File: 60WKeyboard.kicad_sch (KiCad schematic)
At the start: 62 parts, among them IC2 USBLC6-2SC6, J1 USB4215-03-A_REVA, J2 Conn_02x01_MountingPin, J3 Conn_01x04_Socket, U1 PES12-42S-N0024, U3 nRF52840, Y1 ABM11W-32.0000MHZ-7-D1X-T3, Y2 ECS-.327-7-12-TR

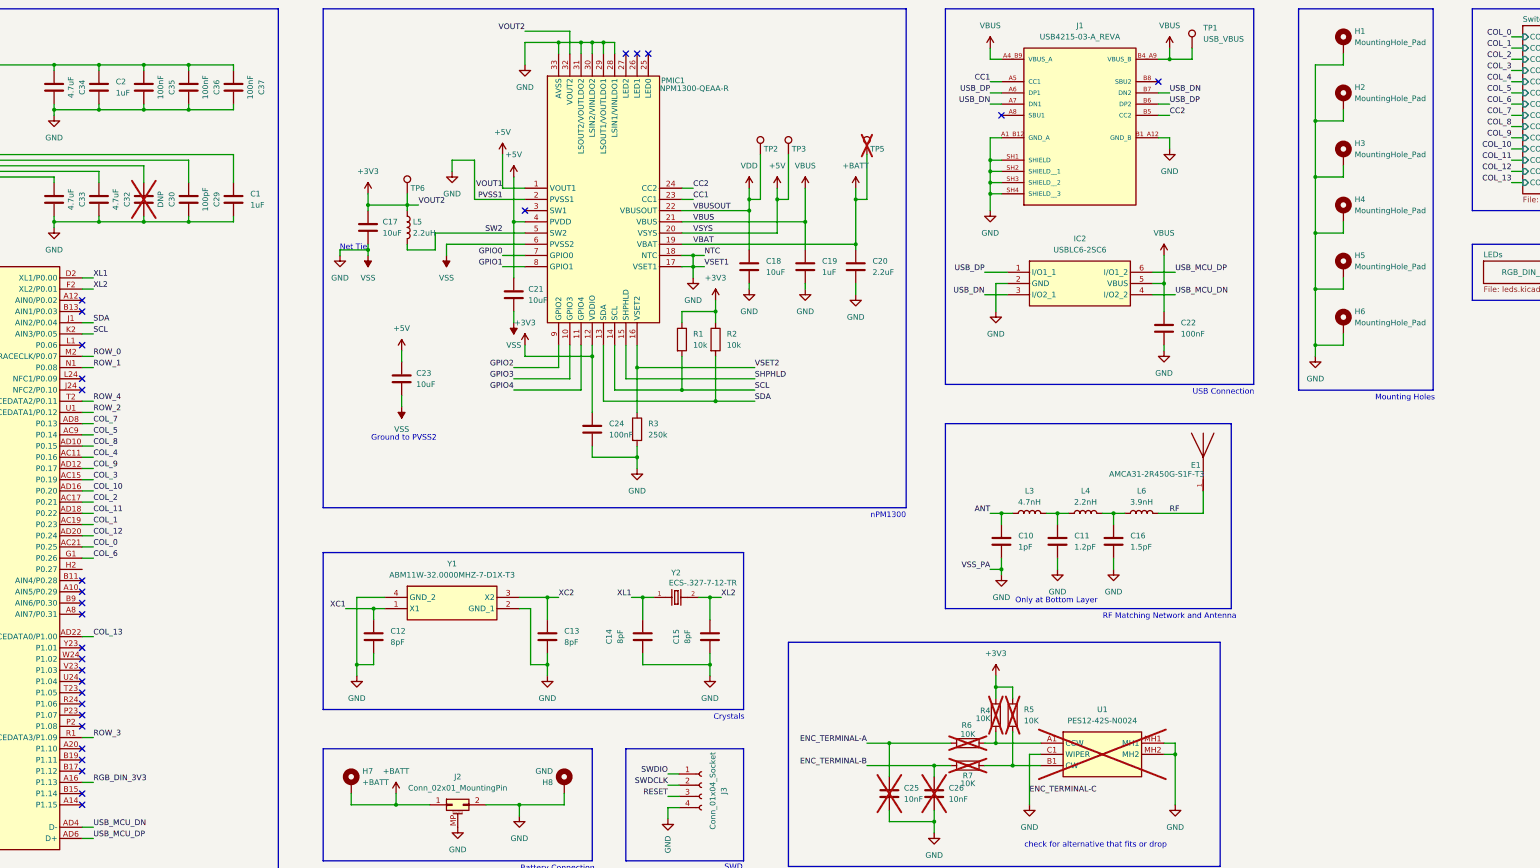
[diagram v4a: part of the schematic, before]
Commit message: Add RGB power control circuit and update PCB
Introduced a new RGB power control circuit using a DMG2301L MOSFET and 10k resistor, connected to the /RGB_POWER net. Updated test point references, modified net assignments, and adjusted routing and vias in the PCB layout. Added and removed backup files and updated production files to reflect the latest design changes.
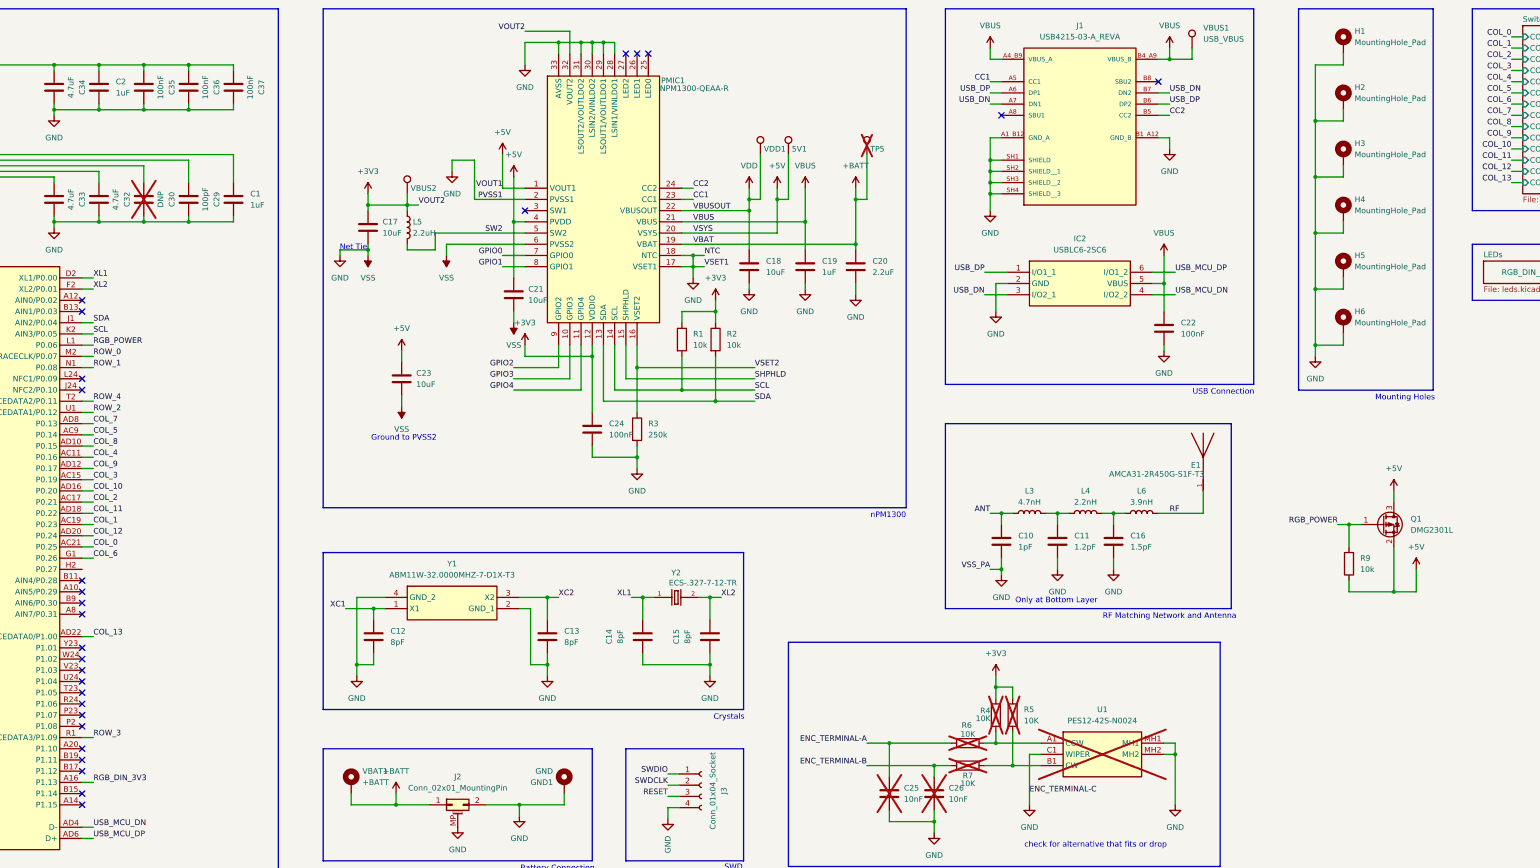
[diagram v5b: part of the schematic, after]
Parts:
- added Q1: DMG2301L, Package_TO_SOT_SMD:SOT-23, symbol Transistor_FET:DMG2301L
- added R9: 10k, Resistor_SMD:R_0402_1005Metric, symbol Device:R
- renumbered TP3 to 5V1, H8 to GND1, H7 to VBAT1, TP1 to VBUS1, TP6 to VBUS2, TP2 to VDD1
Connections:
- net +5V: now also Q1.2 (S), Q1.3 (D), R9.1
- net RGB_POWER: now reaches U3.L1 (P0.06)
- net RGB_POWER: now also Q1.1 (G), R9.2
- no-connect marks 32 -> 31

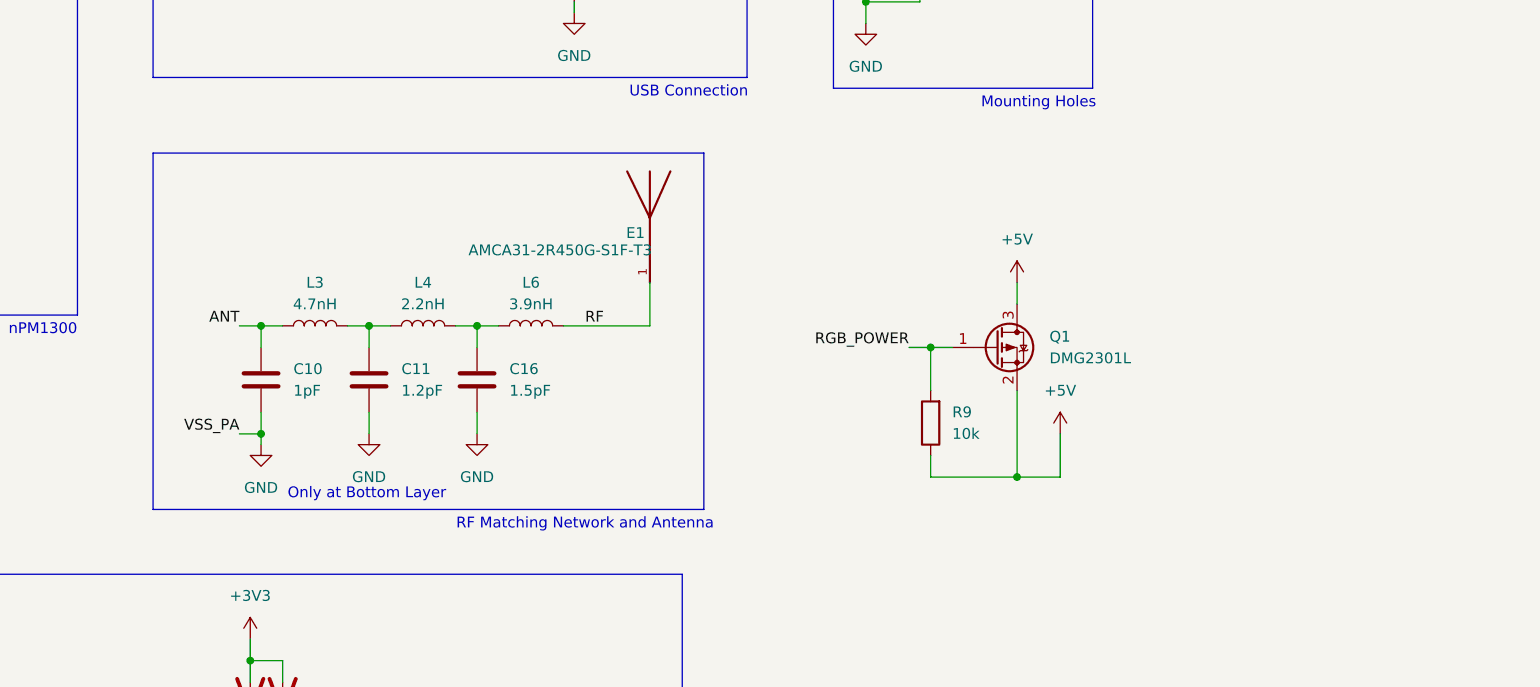
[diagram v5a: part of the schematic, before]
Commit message: Replace RF footprint and add U.FL connector
Replaced the AMCA31-2R450G-S1F-T3 RF footprint with a CONMHF1-SMD-T U.FL connector at the RF output. Updated the S57 keyswitch footprint position. Also updated backup files and production outputs to reflect these changes.
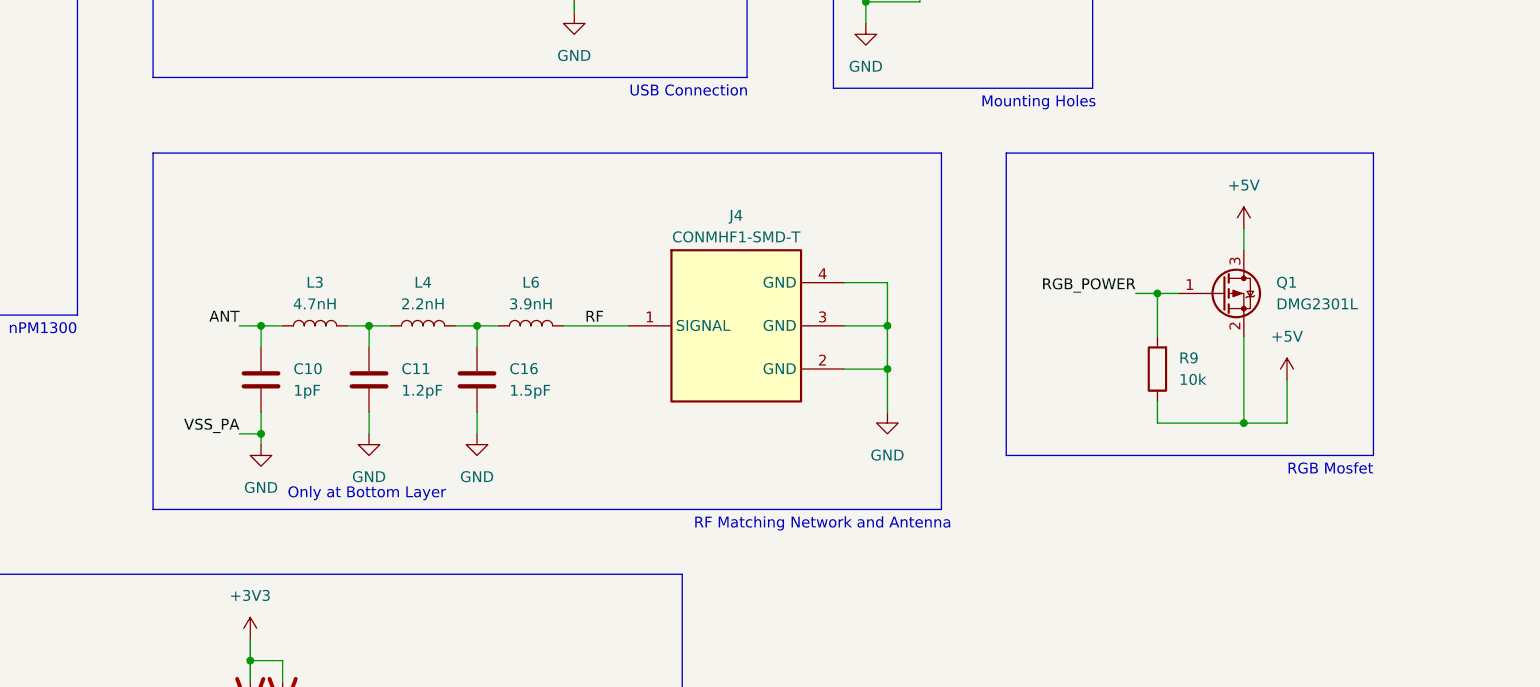
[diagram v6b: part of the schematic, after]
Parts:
- removed E1: AMCA31-2R450G-S1F-T3, SamacSys_Parts:XDCR_AMCA31-2R450G-S1F-T3, symbol AMCA31-2R450G-S1F-T3:AMCA31-2R450G-S1F-T3
- added J4: CONMHF1-SMD-T, CONMHF1SMDT, symbol SamacSys_Parts:CONMHF1-SMD-T
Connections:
- net GND: now also J4.2 (GND), J4.3 (GND), J4.4 (GND)
- net RF: now also J4.1 (SIGNAL)
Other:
- note added: "RGB Mosfet"
- moved on the sheet: Q1, R9

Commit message: Update KiCad project files and backup
Removed autosave and lock files, updated project and schematic files, and renamed backup ZIP. Changed footprint property for connector in schematic and adjusted selection filter for footprints in project settings.
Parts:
- J4: footprint CONMHF1SMDT -> SamacSys_Parts:CONMHF1SMDT
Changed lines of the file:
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@@
 			)
 		)
-		(property "Footprint" "CONMHF1SMDT"
+		(property "Footprint" "SamacSys_Parts:CONMHF1SMDT"
 			(at 434.34 300.66 0)
 			(effects

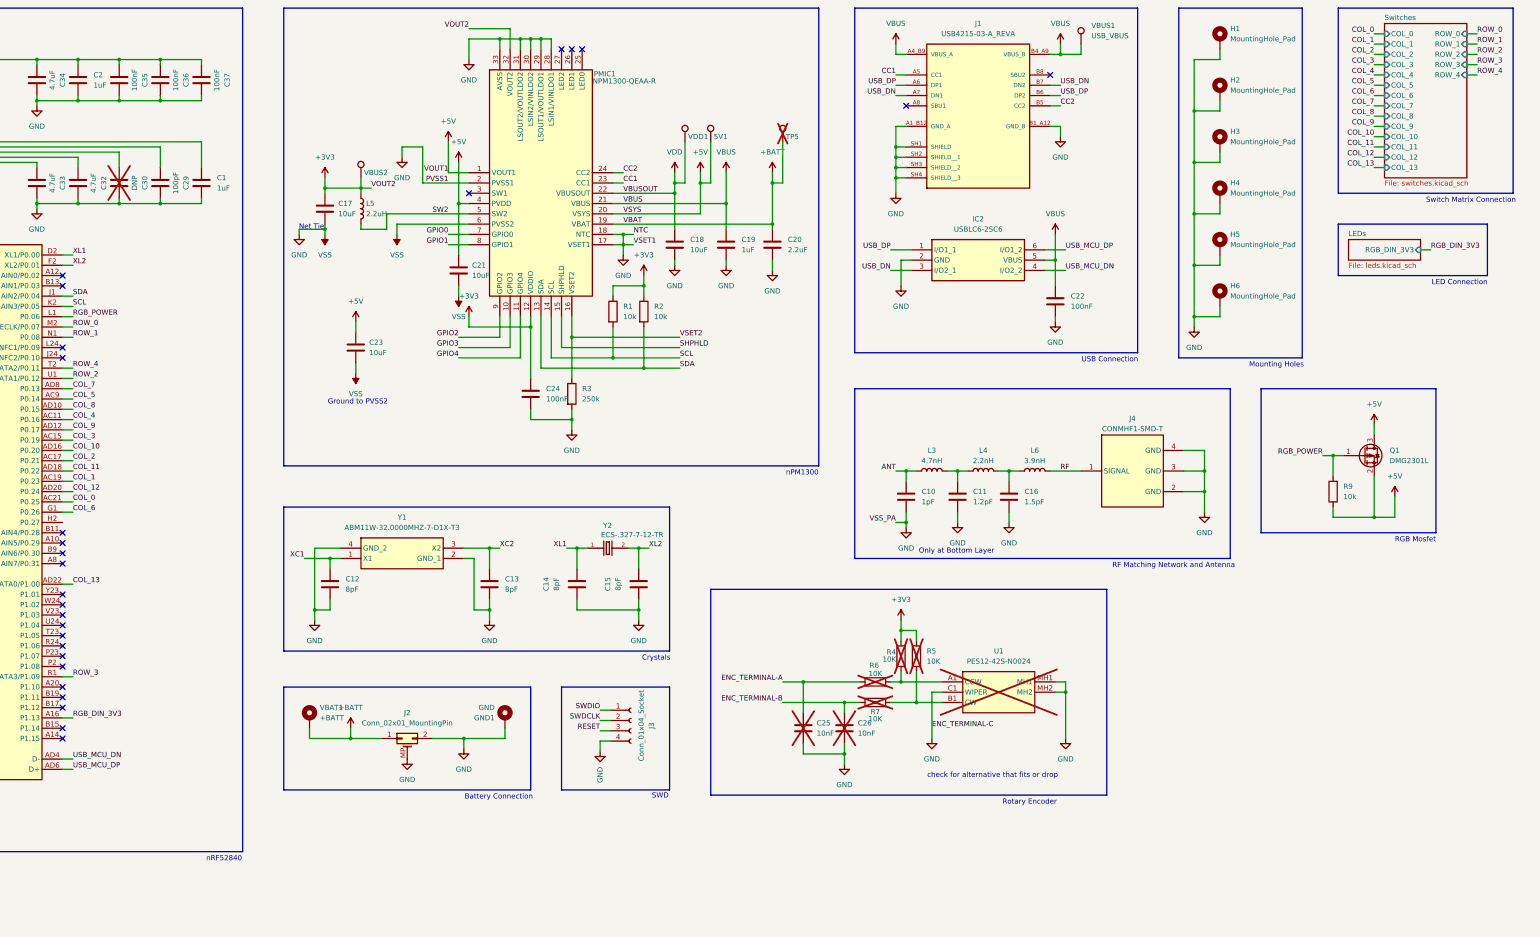
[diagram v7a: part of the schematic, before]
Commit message: v0.4-routing done
need to work on routing and fix it up but preliminary routing done
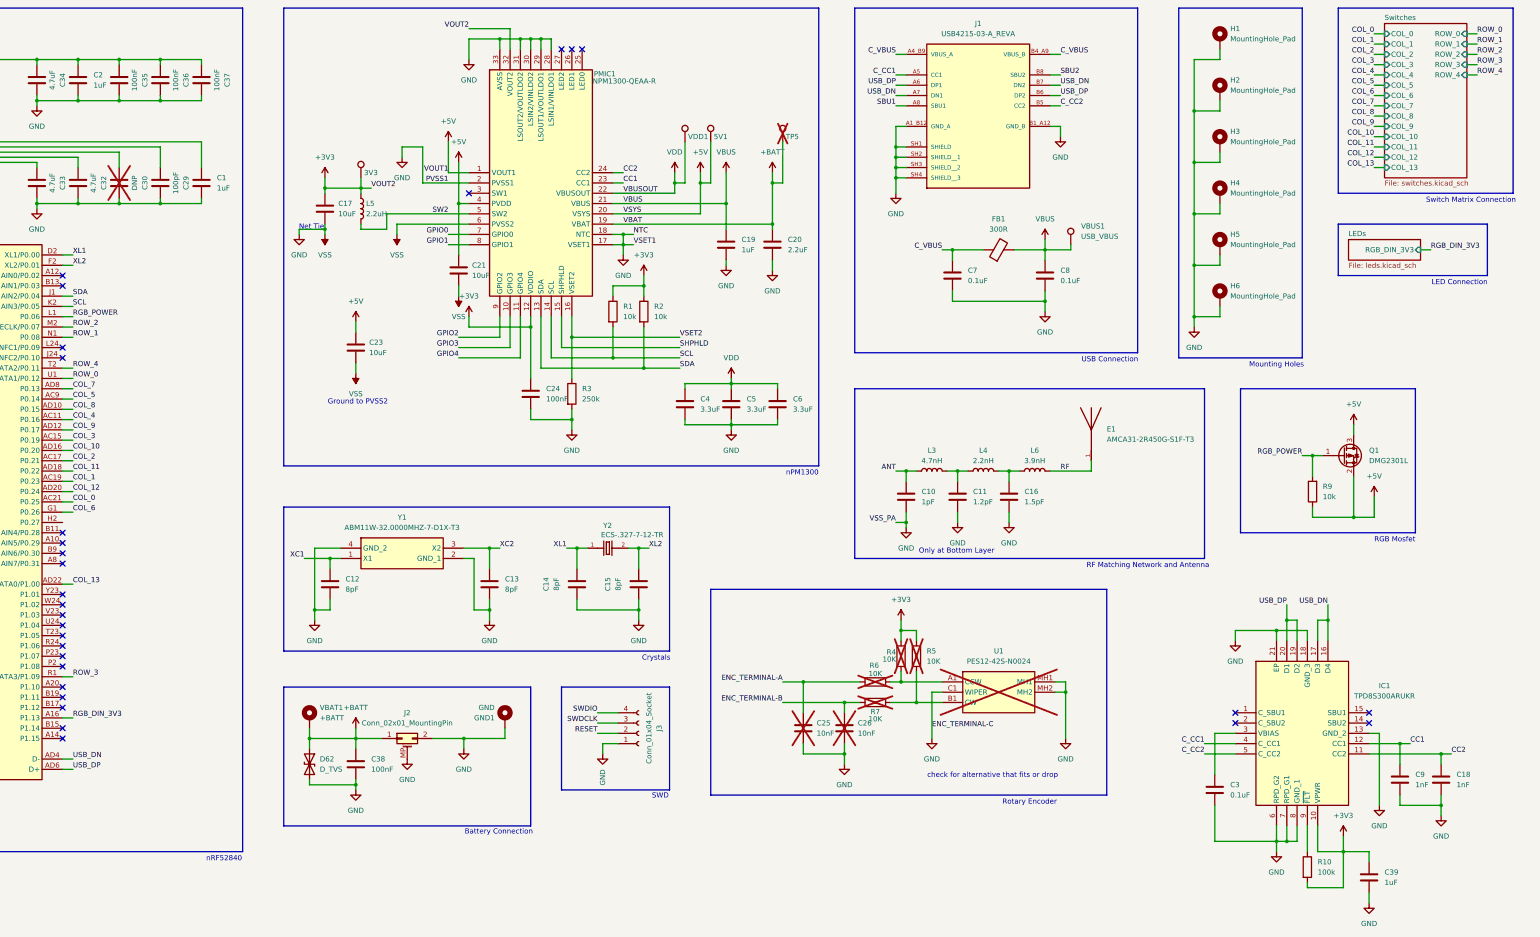
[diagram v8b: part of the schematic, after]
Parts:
- removed C22: 100nF, Capacitor_SMD:C_0402_1005Metric, symbol Device:C
- removed IC2: USBLC6-2SC6, SamacSys_Parts:SOT95P280X145-6N, symbol SamacSys_Parts:USBLC6-2SC6
- removed J4: CONMHF1-SMD-T, SamacSys_Parts:CONMHF1SMDT, symbol SamacSys_Parts:CONMHF1-SMD-T
- added C3, C7, C8: 0.1uF, Capacitor_SMD:C_0402_1005Metric, symbol Device:C
- added C38: 100nF, Capacitor_SMD:C_0402_1005Metric, symbol Device:C
- added C39: 1uF, Capacitor_SMD:C_0402_1005Metric, symbol Device:C
- added C4, C5, C6: 3.3uF, Capacitor_SMD:C_0402_1005Metric, symbol Device:C
- added C9: 1nF, Capacitor_SMD:C_0402_1005Metric, symbol Device:C
- added D62: D_TVS, Diode_SMD:D_SMB, symbol Device:D_TVS
- added E1: AMCA31-2R450G-S1F-T3, SamacSys_Parts:XDCR_AMCA31-2R450G-S1F-T3, symbol AMCA31-2R450G-S1F-T3:AMCA31-2R450G-S1F-T3
- added FB1: 300R, Diode_SMD:D_1206_3216Metric, symbol Device:FerriteBead
- added IC1: TPD8S300ARUKR, SamacSys_Parts:QFN40P300X300X80-21N-D, symbol SamacSys_Parts:TPD8S300ARUKR
- added R10: 100k, Resistor_SMD:R_0402_1005Metric, symbol Device:R
- C18: value 10uF -> 1nF; footprint Capacitor_SMD:C_0603_1608Metric -> Capacitor_SMD:C_0402_1005Metric
- renumbered VBUS2 to 3V3
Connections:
- net USB_MCU_DN is gone; now on net USB_DN: U3.AD4 (D-)
- net USB_MCU_DP is gone; now on net USB_DP: U3.AD6 (D+)
- net +3V3: now also C39.1, IC1.10 (VPWR), R10.2
- net +BATT: now also C38.1, D62.1 (A1)
- net CC1: now also C9.1, IC1.12 (CC1); no longer J1.A5 (CC1)
- net CC2: now also C18.1, IC1.11 (CC2); no longer J1.B5 (CC2)
- net GND: now also J3.1 (Pin_1), C3.2, C38.2, C39.2, C4.2, C5.2, C6.2, C7.2, C8.2, C9.2, D62.2 (A2), IC1.13 (GND_2), IC1.18 (GND_3), IC1.21 (EP), IC1.6 (RPD_G2), IC1.7 (RPD_G1), IC1.8 (GND_1); no longer J3.4 (Pin_4)
- net RESET: now also J3.2 (Pin_2); no longer J3.3 (Pin_3)
- net RF: now also E1.1
- net ROW_0: now also U3.U1 (TRACEDATA1/P0.12); no longer U3.M2 (TRACECLK/P0.07)
- net ROW_2: now also U3.M2 (TRACECLK/P0.07); no longer U3.U1 (TRACEDATA1/P0.12)
- net SWDCLK: now also J3.3 (Pin_3); no longer J3.2 (Pin_2)
- net SWDIO: now also J3.4 (Pin_4); no longer J3.1 (Pin_1)
- net USB_DN: now also IC1.16 (D4), IC1.17 (D3)
- net USB_DP: now also IC1.19 (D2), IC1.20 (D1)
- net VBUS: now also C8.1, FB1.2; no longer J1.A4_B9 (VBUS_A), J1.B4_A9 (VBUS_B)
- net VDD: now also C4.1, C5.1, C6.1; no longer C18.1
- net SBU1: now reaches J1.A8 (SBU1)
- net SBU2: now reaches J1.B8 (SBU2)
- new net: C3.1, IC1.3 (VBIAS)
- new net: IC1.9 (~{FLT}), R10.1
- new net C_CC1: IC1.4 (C_CC1), J1.A5 (CC1)
- new net C_CC2: IC1.5 (C_CC2), J1.B5 (CC2)
- new net C_VBUS: C7.1, FB1.1, J1.A4_B9 (VBUS_A), J1.B4_A9 (VBUS_B)
- no-connect marks 31 -> 33
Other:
- moved on the sheet: J3, Q1, R9, VBUS1
